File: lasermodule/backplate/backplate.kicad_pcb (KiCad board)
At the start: 2 copper layers, 25.2 x 55.1 mm, 2 parts

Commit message: simplified loading in freecad, updated pcbs
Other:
- board text added: "PCB3D_BR_backplate"
- board text added: "PCB3D_TL_backplate"

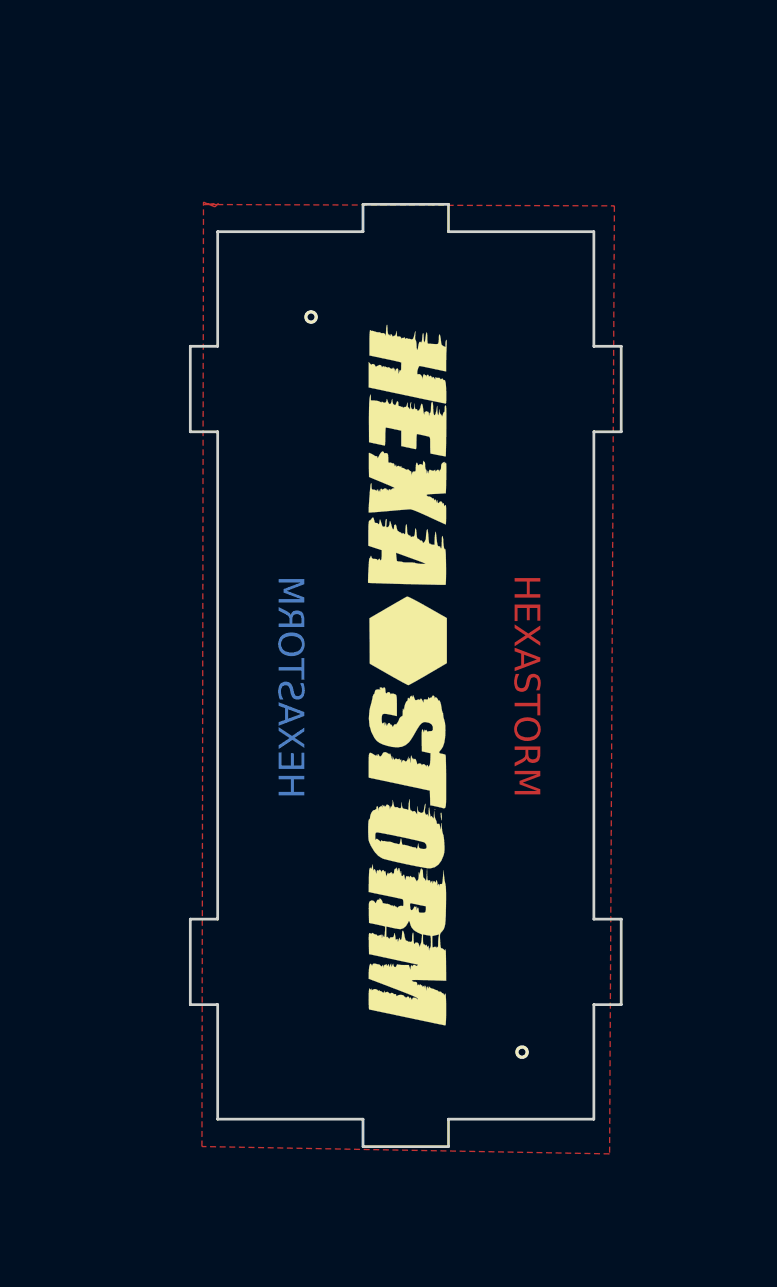
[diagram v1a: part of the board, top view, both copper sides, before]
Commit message: pcbs can be rendered
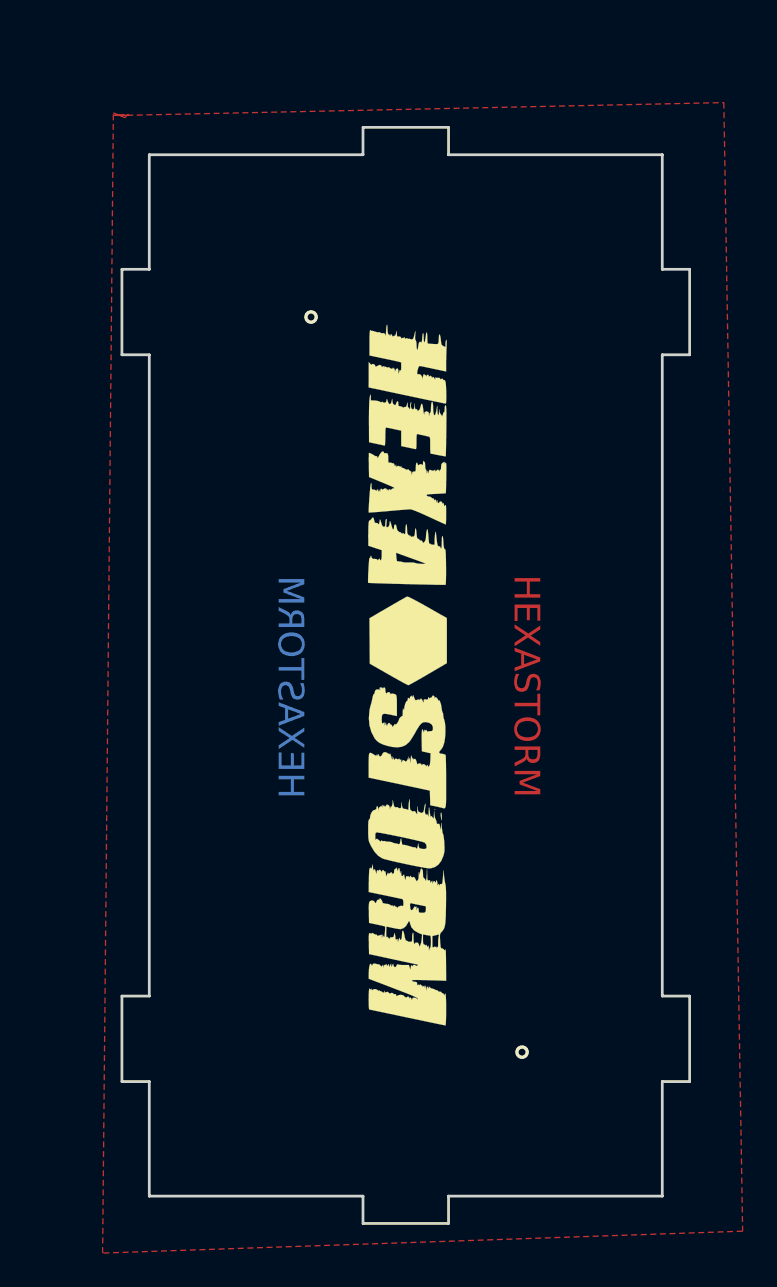
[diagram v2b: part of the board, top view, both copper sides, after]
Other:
- board size 25.2 x 55.1 mm -> 33.2 x 64.1 mm
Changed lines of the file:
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@@
       (stroke (width 0.01) (type solid)) (fill solid) (layer "B.SilkS"))
   )
-  (gr_line (start 141.514 89.7) (end 141.514 84.7)
+  (gr_line (start 151.6145 134.3995) (end 139.1145 134.3995)
     (stroke (width 0.16) (type solid)) (layer "Edge.Cuts"))
-  (gr_line (start 165.114 118.2) (end 166.714 118.2)
+  (gr_line (start 169.1145 73.4995) (end 169.1145 80.1995)
     (stroke (width 0.16) (type solid)) (layer "Edge.Cuts"))
-  (gr_line (start 165.114 89.7) (end 165.114 118.2)
+  (gr_line (start 151.6145 73.4995) (end 151.6145 71.8995)
     (stroke (width 0.16) (type solid)) (layer "Edge.Cuts"))
-  (gr_line (start 156.614 129.899) (end 156.614 131.5)
+  (gr_line (start 170.7145 127.6995) (end 169.1145 127.6995)
     (stroke (width 0.16) (type solid)) (layer "Edge.Cuts"))
-  (gr_line (start 143.114 77.999) (end 151.614 77.999)
+  (gr_line (start 137.5145 127.6995) (end 137.5145 122.6995)
     (stroke (width 0.16) (type solid)) (layer "Edge.Cuts"))
-  (gr_line (start 156.614 131.5) (end 151.614 131.5)
+  (gr_line (start 169.1145 80.1995) (end 170.7145 80.1995)
     (stroke (width 0.16) (type solid)) (layer "Edge.Cuts"))
-  (gr_line (start 143.114 77.999) (end 143.114 84.7)
+  (gr_line (start 169.1145 85.1995) (end 169.1145 122.6995)
     (stroke (width 0.16) (type solid)) (layer "Edge.Cuts"))
-  (gr_line (start 165.114 84.7) (end 166.714 84.7)
+  (gr_line (start 137.5145 122.6995) (end 139.1145 122.6995)
     (stroke (width 0.16) (type solid)) (layer "Edge.Cuts"))
-  (gr_line (start 151.614 131.5) (end 151.614 129.899)
+  (gr_line (start 170.7145 85.1995) (end 169.1145 85.1995)
     (stroke (width 0.16) (type solid)) (layer "Edge.Cuts"))
-  (gr_line (start 143.114 89.7) (end 143.114 118.2)
+  (gr_line (start 156.6145 71.8995) (end 156.6145 73.4995)
     (stroke (width 0.16) (type solid)) (layer "Edge.Cuts"))
-  (gr_line (start 156.614 77.999) (end 165.114 77.999)
+  (gr_line (start 169.1145 122.6995) (end 170.7145 122.6995)
     (stroke (width 0.16) (type solid)) (layer "Edge.Cuts"))
-  (gr_line (start 166.714 89.7) (end 165.114 89.7)
+  (gr_line (start 139.1145 127.6995) (end 137.5145 127.6995)
     (stroke (width 0.16) (type solid)) (layer "Edge.Cuts"))
-  (gr_line (start 156.614 76.4) (end 156.614 77.999)
+  (gr_line (start 170.7145 122.6995) (end 170.7145 127.6995)
     (stroke (width 0.16) (type solid)) (layer "Edge.Cuts"))
-  (gr_line (start 141.514 118.2) (end 143.114 118.2)
+  (gr_line (start 156.6145 134.3995) (end 156.6145 135.9995)
     (stroke (width 0.16) (type solid)) (layer "Edge.Cuts"))
-  (gr_line (start 143.114 89.7) (end 141.514 89.7)
+  (gr_line (start 169.1145 134.3995) (end 156.6145 134.3995)
     (stroke (width 0.16) (type solid)) (layer "Edge.Cuts"))
-  (gr_line (start 143.114 123.2) (end 141.514 123.2)
+  (gr_line (start 156.6145 73.4995) (end 169.1145 73.4995)
     (stroke (width 0.16) (type solid)) (layer "Edge.Cuts"))
-  (gr_line (start 166.714 118.2) (end 166.714 123.2)
+  (gr_line (start 170.7145 80.1995) (end 170.7145 85.1995)
     (stroke (width 0.16) (type solid)) (layer "Edge.Cuts"))
-  (gr_line (start 141.514 123.2) (end 141.514 118.2)
+  (gr_line (start 151.6145 135.9995) (end 151.6145 134.3995)
     (stroke (width 0.16) (type solid)) (layer "Edge.Cuts"))
-  (gr_line (start 151.614 77.999) (end 151.614 76.4)
+  (gr_line (start 139.1145 85.1995) (end 137.5145 85.1995)
     (stroke (width 0.16) (type solid)) (layer "Edge.Cuts"))
-  (gr_line (start 165.114 129.899) (end 156.614 129.899)
+  (gr_line (start 137.5145 85.1995) (end 137.5145 80.1995)
     (stroke (width 0.16) (type solid)) (layer "Edge.Cuts"))
-  (gr_line (start 141.514 84.7) (end 143.114 84.7)
+  (gr_line (start 156.6145 135.9995) (end 151.6145 135.9995)
     (stroke (width 0.16) (type solid)) (layer "Edge.Cuts"))
-  (gr_line (start 166.714 84.7) (end 166.714 89.7)
+  (gr_line (start 137.5145 80.1995) (end 139.1145 80.1995)
     (stroke (width 0.16) (type solid)) (layer "Edge.Cuts"))
-  (gr_line (start 165.114 77.999) (end 165.114 84.7)
+  (gr_line (start 169.1145 127.6995) (end 169.1145 134.3995)
     (stroke (width 0.16) (type solid)) (layer "Edge.Cuts"))
-  (gr_line (start 151.614 76.4) (end 156.614 76.4)
+  (gr_line (start 139.1145 127.6995) (end 139.1145 134.3995)
     (stroke (width 0.16) (type solid)) (layer "Edge.Cuts"))
-  (gr_line (start 143.114 123.2) (end 143.114 129.899)
+  (gr_line (start 139.1145 73.4995) (end 139.1145 80.1995)
     (stroke (width 0.16) (type solid)) (layer "Edge.Cuts"))
-  (gr_line (start 165.114 123.2) (end 165.114 129.899)
+  (gr_line (start 139.1145 85.1995) (end 139.1145 122.6995)
     (stroke (width 0.16) (type solid)) (layer "Edge.Cuts"))
-  (gr_line (start 166.714 123.2) (end 165.114 123.2)
+  (gr_line (start 139.1145 73.4995) (end 151.6145 73.4995)
     (stroke (width 0.16) (type solid)) (layer "Edge.Cuts"))
-  (gr_line (start 151.614 129.899) (end 143.114 129.899)
+  (gr_line (start 151.6145 71.8995) (end 156.6145 71.8995)
     (stroke (width 0.16) (type solid)) (layer "Edge.Cuts"))
   (gr_text "HEXASTORM" (at 161.1745 104.5795 270) (layer "F.Cu")
@@
     (effects (font (size 1 1) (thickness 0.15)))
   )
-  (gr_text "PCB3D_BR_backplate" (at 151.5745 134.4295) (layer "Cmts.User")
+  (gr_text "PCB3D_BR_backplate" (at 174.2145 138.0495) (layer "Cmts.User")
     (effects (font (size 1 1) (thickness 0.15)) (justify left bottom))
   )
-  (gr_text "PCB3D_TL_backplate" (at 141.4145 76.0095) (layer "Cmts.User")
+  (gr_text "PCB3D_TL_backplate" (at 135.9145 69.6495) (layer "Cmts.User")
     (effects (font (size 1 1) (thickness 0.15)) (justify left bottom))
   )
@@
     (polygon
       (pts
-        (xy 142.578096 76.392197)
-        (xy 142.3445 76.4095)
-        (xy 142.621714 76.410425)
-        (xy 142.9545 76.5495)
-        (xy 143.092005 76.411995)
-        (xy 142.621714 76.410425)
-        (xy 142.578096 76.392197)
-        (xy 143.1545 76.3495)
-        (xy 143.092005 76.411995)
-        (xy 166.3145 76.4895)
-        (xy 166.0345 131.9295)
-        (xy 142.1945 131.4995)
-        (xy 142.2845 76.2695)
+        (xy 137.308096 71.172197)
+        (xy 137.0745 71.1895)
+        (xy 137.351714 71.190425)
+        (xy 137.6845 71.3295)
+        (xy 137.822005 71.191995)
+        (xy 137.351714 71.190425)
+        (xy 137.308096 71.172197)
+        (xy 137.8845 71.1295)
+        (xy 137.822005 71.191995)
+        (xy 172.7145 70.4495)
+        (xy 173.8145 136.4495)
+        (xy 136.3845 137.7295)
+        (xy 137.0145 71.0495)
       )
     )

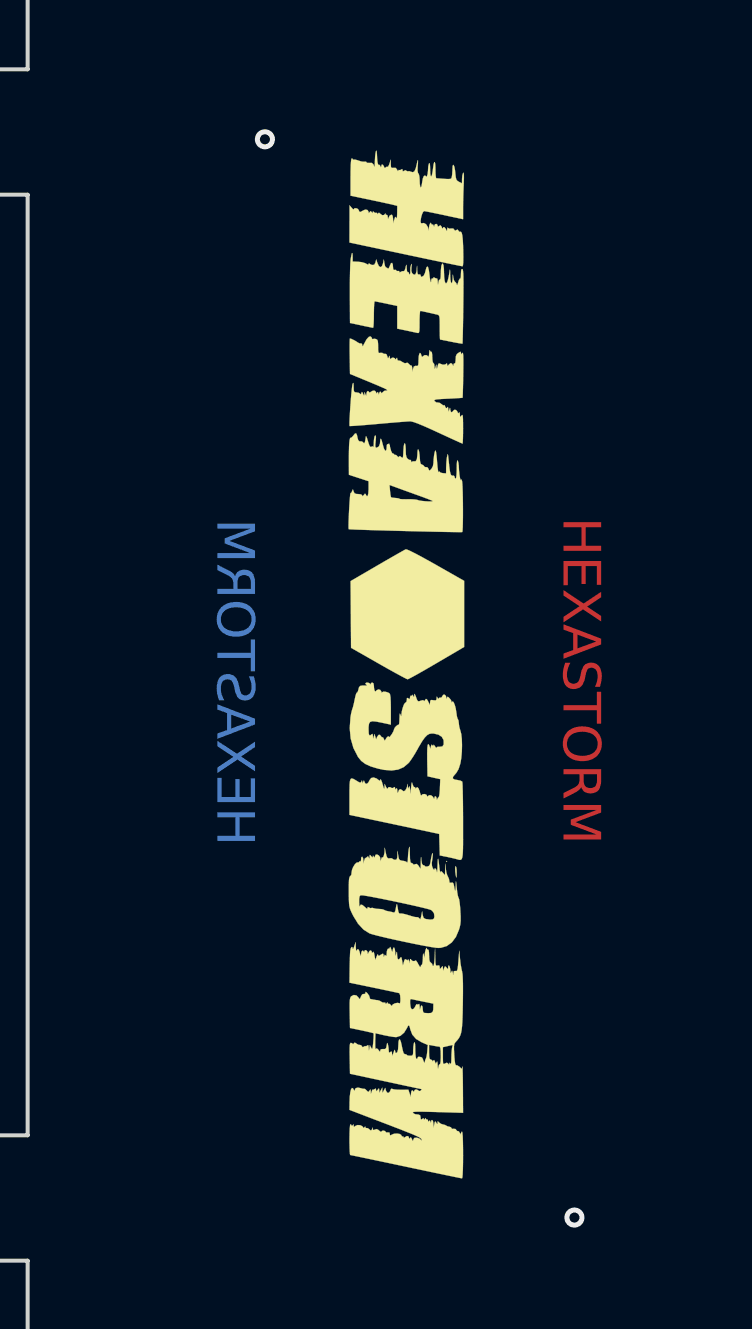
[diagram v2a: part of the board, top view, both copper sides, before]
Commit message: changed position logos
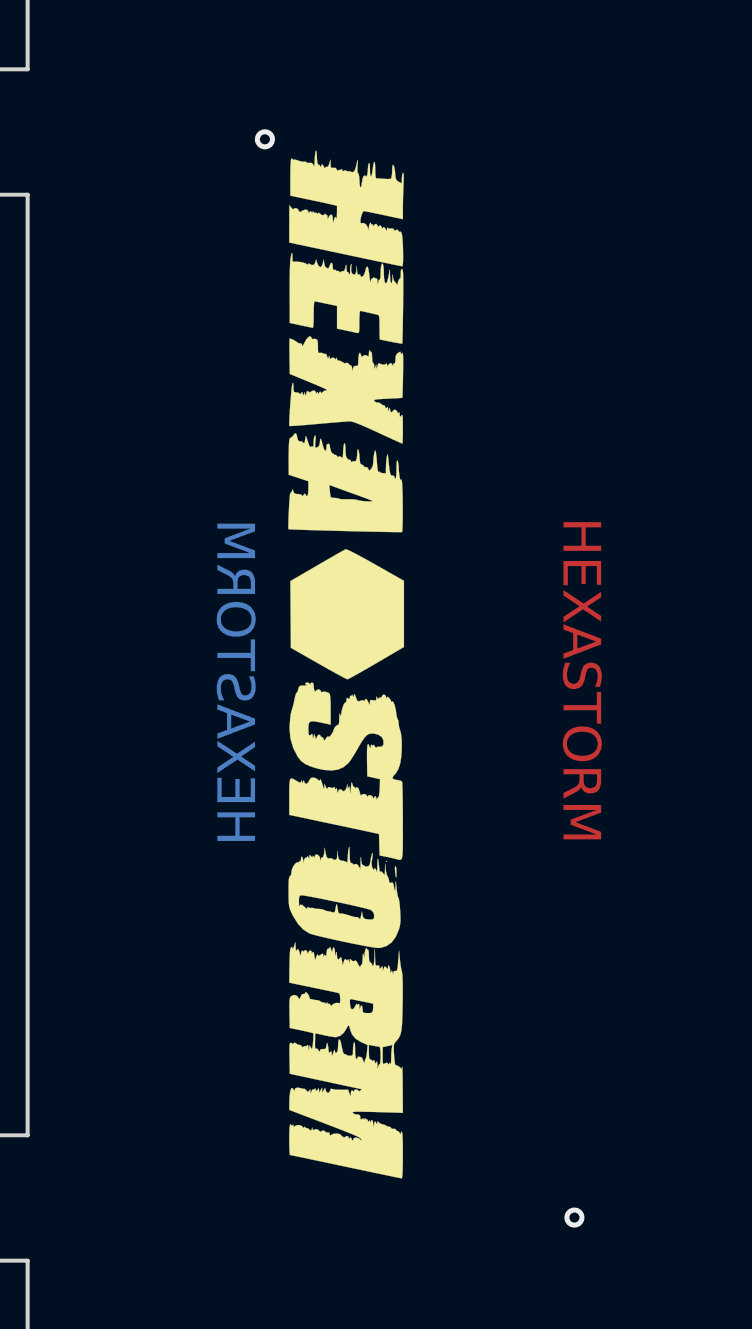
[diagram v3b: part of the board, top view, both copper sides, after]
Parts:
- moved L1 2.40 mm to (151.8, 103.9)
- moved L2 2.29 mm to (151.8, 104.4)
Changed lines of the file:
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@@
   (net 0 "")
   (footprint "footprints:hexastorm" (layer "F.Cu")
-    (at 154.23134 103.886 -90)
+    (at 151.83134 103.886 -90)
     (attr through_hole)
     (fp_text reference "L1" (at -0.67818 0.92964 90) (layer "F.SilkS") hide
         (effects (font (size 1.524 1.524) (thickness 0.3)))
     )
-    (fp_text value "Logo_Open_Hardware_Large" (at 1.31826 0.21844 -90) (layer "F.SilkS") hide
+    (fp_text value "Logo_Open_Hardware_Large" (at 1.31826 0.21844 90) (layer "F.SilkS") hide
         (effects (font (size 1.524 1.524) (thickness 0.3)))
     )
@@
   )
   (footprint "footprints:hexastorm" (layer "B.Cu")
-    (at 154.12212 104.43464 90)
+    (at 151.83134 104.43464 90)
     (attr through_hole)
     (fp_text reference "L2" (at 0 0 90) (layer "B.SilkS") hide
